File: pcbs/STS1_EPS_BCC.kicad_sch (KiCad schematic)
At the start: 40 parts, among them Q1 SI7135DP-T1-GE3, U1 LTC4020EUHFPBF, U2 SI7272DP-T1-GE3, U3 SI7272DP-T1-GE3

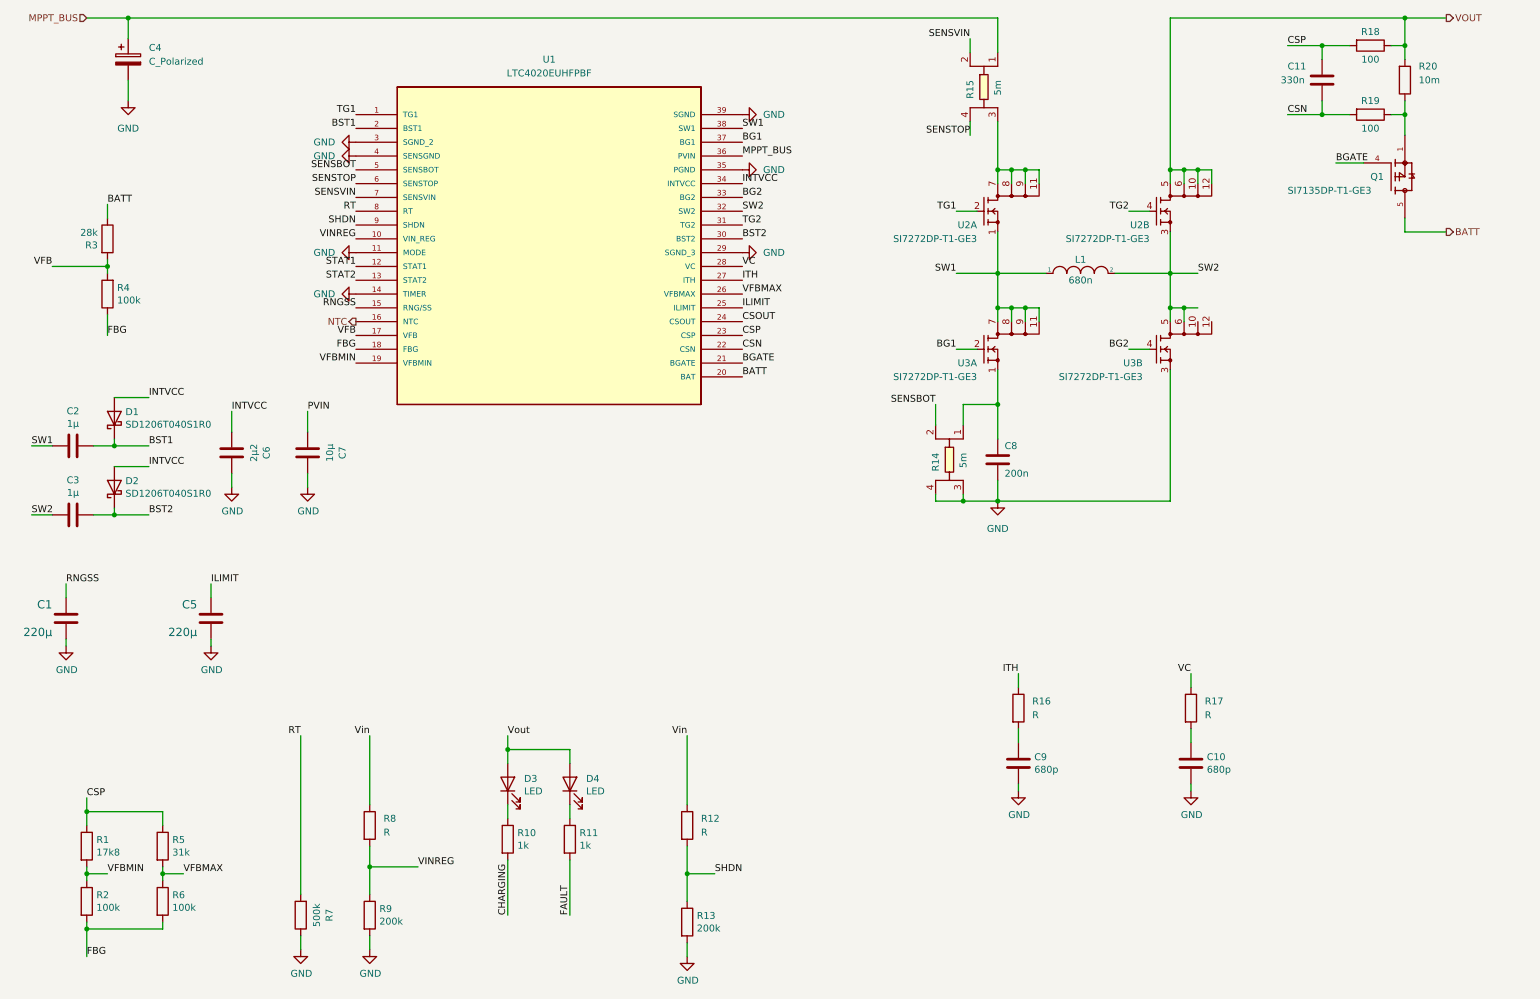
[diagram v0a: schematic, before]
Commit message: Worked on STS1_EPS_1.
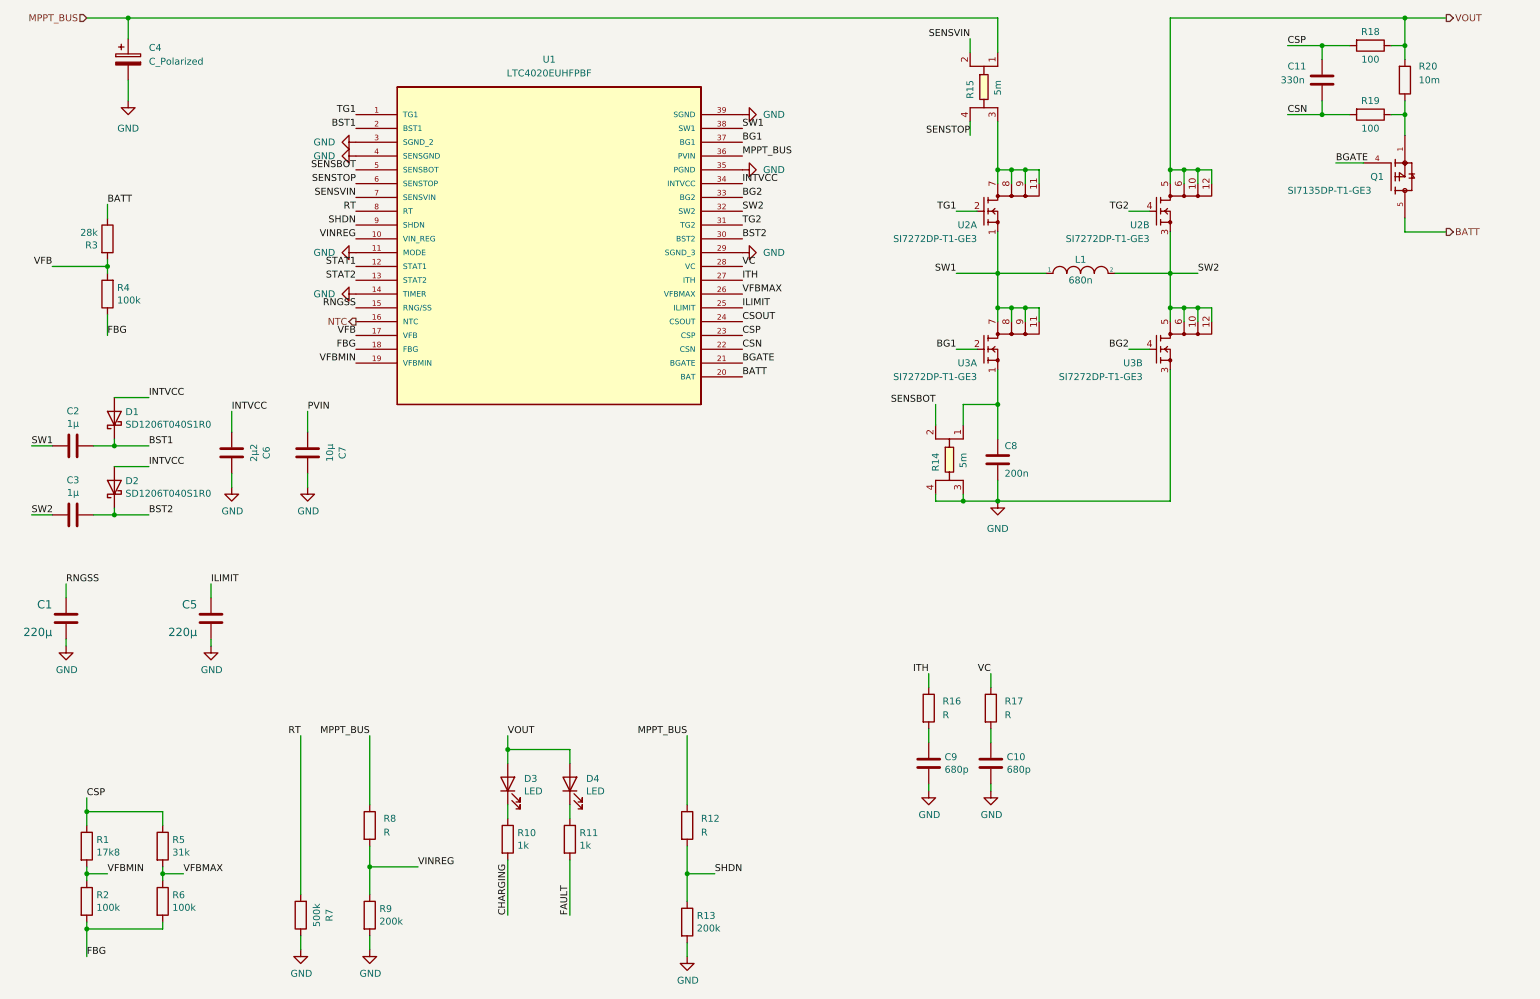
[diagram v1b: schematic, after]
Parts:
- Q1: footprint footprints:TRANS_SI7135DP-T1-GE3 -> STS_Package_SO:POWERPAK_SO8_single
- R16, R17: footprint (none) -> Resistor_SMD:R_0805_2012Metric
- U1: footprint QFN-38_UHF -> STS_Package_DFN_QFN:AD_QFN-38_UHF
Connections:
- net Vin is gone; now on net MPPT_BUS: R12.1, R8.1
- net Vout is gone; now on net VOUT: D3.2 (A), D4.2 (A)
- net SW2: now also U3.10 (D2_3), U3.12 (D2_4)
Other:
- moved on the sheet: C10, C9, R16, R17

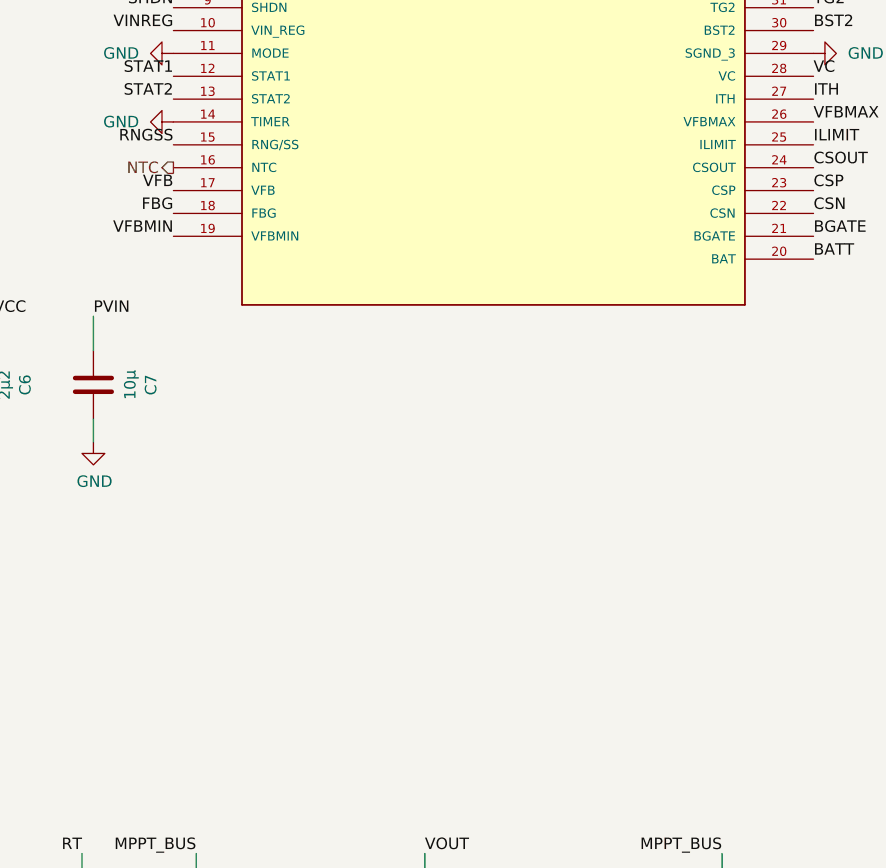
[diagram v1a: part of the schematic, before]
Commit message: Worked on STS1_EPS_1.
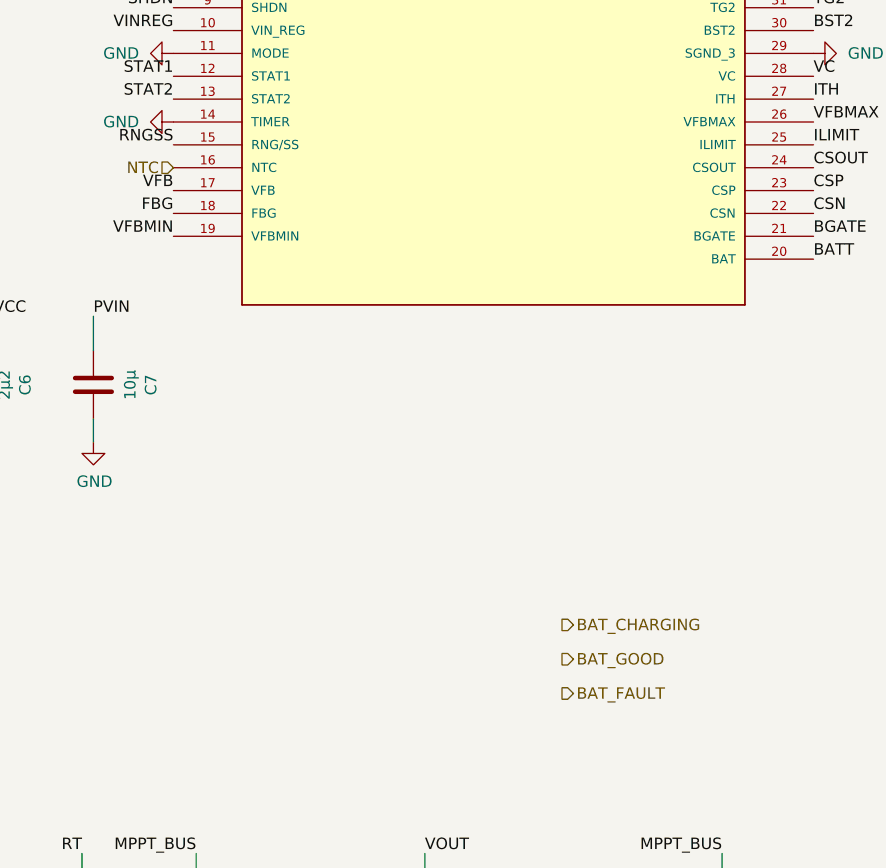
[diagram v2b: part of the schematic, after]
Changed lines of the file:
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@@
     (effects (font (size 1.27 1.27)) (justify left bottom))
+  )
+  (hierarchical_label "BAT_GOOD" (shape output) (at 118.11 127 0)
+    (effects (font (size 1.27 1.27)) (justify left))
   )
   (hierarchical_label "VOUT" (shape output) (at 275.59 16.51 0)
@@
     (effects (font (size 1.27 1.27)) (justify right))
   )
-  (hierarchical_label "NTC" (shape output) (at 74.93 72.39 180)
+  (hierarchical_label "NTC" (shape input) (at 74.93 72.39 180)
     (effects (font (size 1.27 1.27)) (justify right))
   )
+  (hierarchical_label "BAT_CHARGING" (shape output) (at 118.11 123.19 0)
+    (effects (font (size 1.27 1.27)) (justify left))
+  )
+  (hierarchical_label "BAT_FAULT" (shape output) (at 118.11 130.81 0)
+    (effects (font (size 1.27 1.27)) (justify left))
+  )
   (hierarchical_label "BATT" (shape output) (at 275.59 55.88 0)

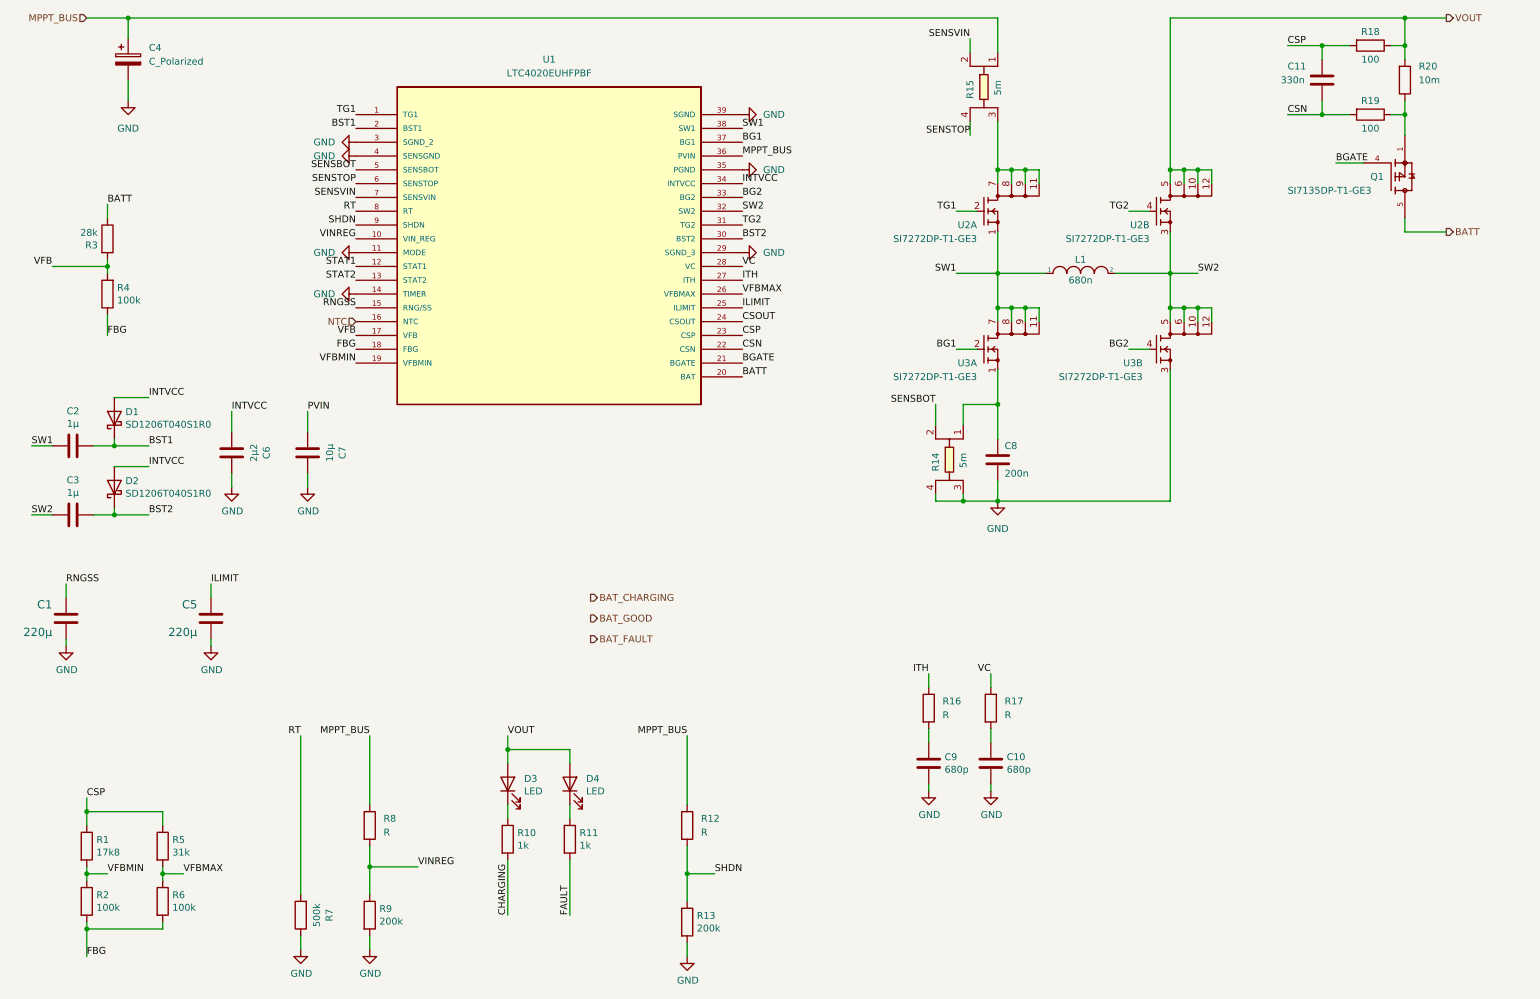
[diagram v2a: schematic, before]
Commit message: Worked on STS_EPS_1.
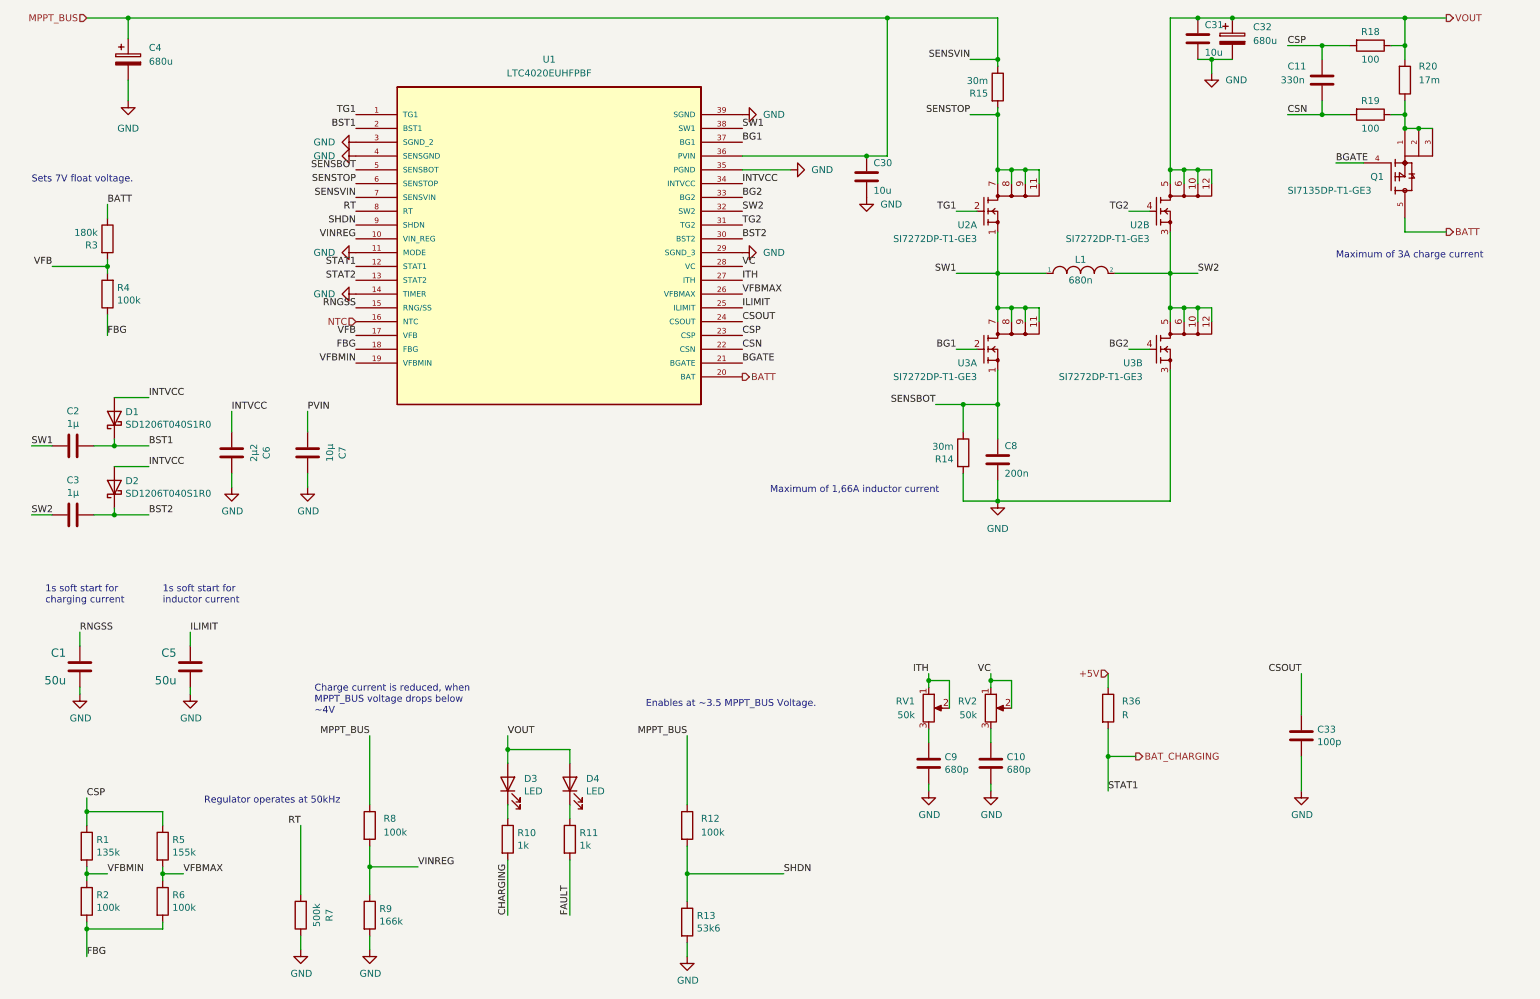
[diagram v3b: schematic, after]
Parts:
- removed R14, R15: 5m, footprints:CST0612-FC-R002E, symbol 2021-06-29_19-28-22:CST0612-FC-R002E
- removed R16, R17: R, Resistor_SMD:R_0805_2012Metric, symbol Device:R
- added C30, C31: 10u, Capacitor_SMD:C_0805_2012Metric, symbol Device:C
- added C32: 680u, symbol Device:C_Polarized
- added C33: 100p, Capacitor_SMD:C_0805_2012Metric, symbol Device:C
- added R14, R15: 30m, Resistor_SMD:R_0805_2012Metric, symbol Device:R
- added R36: R, Resistor_SMD:R_0805_2012Metric, symbol Device:R
- added RV1, RV2: 50k, Potentiometer_SMD:Potentiometer_Bourns_TC33X_Vertical, symbol Device:R_Potentiometer
- C1, C5: value 220µ -> 50u
- C4: value C_Polarized -> 680u
- L1: footprint footprints:INDPM7366X500N -> Inductor_SMD:L_10.4x10.4_H4.8
- Q1: symbol SI7135DP-T1-GE3:SI7135DP-T1-GE3 -> STS_Transistor_FET:SI7135DP-T1-GE3
- R1: value 17k8 -> 135k
- R12, R8: value R -> 100k; footprint (none) -> Resistor_SMD:R_0805_2012Metric
- R13: value 200k -> 53k6
- R20: value 10m -> 17m
- R3: value 28k -> 180k
- R5: value 31k -> 155k
- R9: value 200k -> 166k
- U2, U3: footprint SI7288DPT1GE3 -> STS_Package_SO:POWERPAK_SO8; symbol SI7272DP-T1-GE3:SI7272DP-T1-GE3 -> STS_Transistor_FET:SI7272DP-T1-GE3
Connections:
- net SENSVIN is gone; now on net MPPT_BUS: U1.7 (SENSVIN)
- net STAT1 is gone; now on net BAT_CHARGING: U1.12 (STAT1)
- net BAT_CHARGING: now also R36.2
- net CSOUT: now also C33.1
- net GND: now also C30.1, C31.1, C32.2, C33.2, R14.2
- net ITH: now also RV1.1, RV1.2
- net MPPT_BUS: now also C30.2, R15.1
- net SENSBOT: now also C8.2, U3.1 (S1), R14.1
- net SENSTOP: now also U2.11 (D1_4), U2.7 (D1_1), U2.8 (D1_2), U2.9 (D1_3), R15.2
- net VC: now also RV2.1, RV2.2
- net VOUT: now also C31.2, C32.1
- net at C9.1: now also RV1.3
- net at C10.1: now also RV2.3
- net at Q1.1, R19.1, R20.1: now also Q1.2, Q1.3
- new net +5V: R36.1
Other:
- note added: "1s soft start for charging current"
- note added: "1s soft start for inductor current"
- note added: "Charge current is reduced, when MPPT_BUS voltage drops below ~4V"
- note added: "Enables at ~3.5 MPPT_BUS Voltage."
- note added: "Maximum of 1,66A inductor current"
- note added: "Maximum of 3A charge current"
- note added: "Regulator operates at 50kHz"
- note added: "Sets 7V float voltage."
- moved on the sheet: C1, C5
